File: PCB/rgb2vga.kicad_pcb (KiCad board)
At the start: 2 copper layers, 73.7 x 55.9 mm, 41 parts, among them U1 LM1881

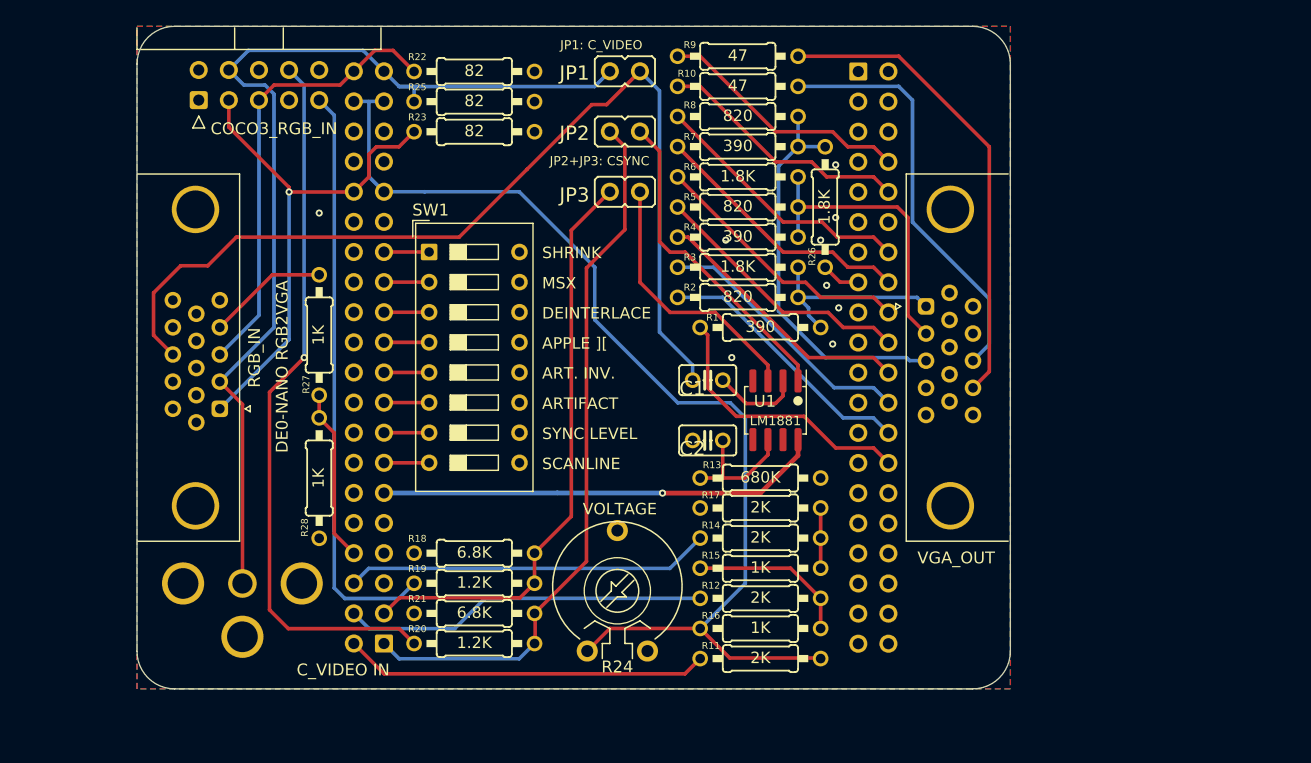
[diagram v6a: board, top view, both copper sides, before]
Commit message: layout grid alignmen
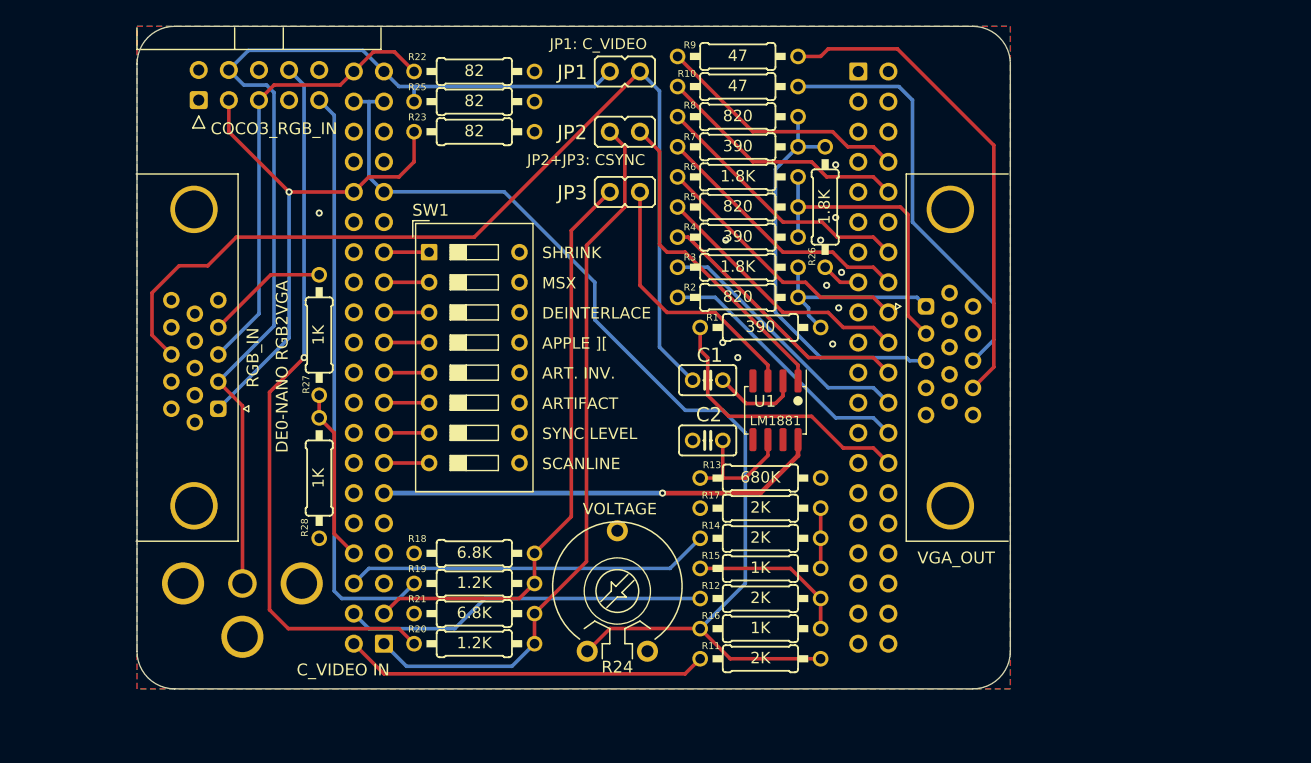
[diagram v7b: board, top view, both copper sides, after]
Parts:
- moved RGB_IN 0.13 mm to (109.2, 105.3)
- turned JP2 to 90 degrees
- turned JP3 to 90 degrees
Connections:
- JP2 pad 1: _HSYNC -> N$3
- JP2 pad 2: N$3 -> _HSYNC
- JP3 pad 1: _VSYNC -> N$2
- JP3 pad 2: N$2 -> _VSYNC
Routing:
- net DIFF_N: track 92.5 -> 91.1 mm
- net _VS: track 40.2 -> 41.3 mm
- net DIFFG: track 85.7 -> 84.7 mm
- net GND: vias 9 -> 11

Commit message: link schematic to pcb, remove unused footprints and models
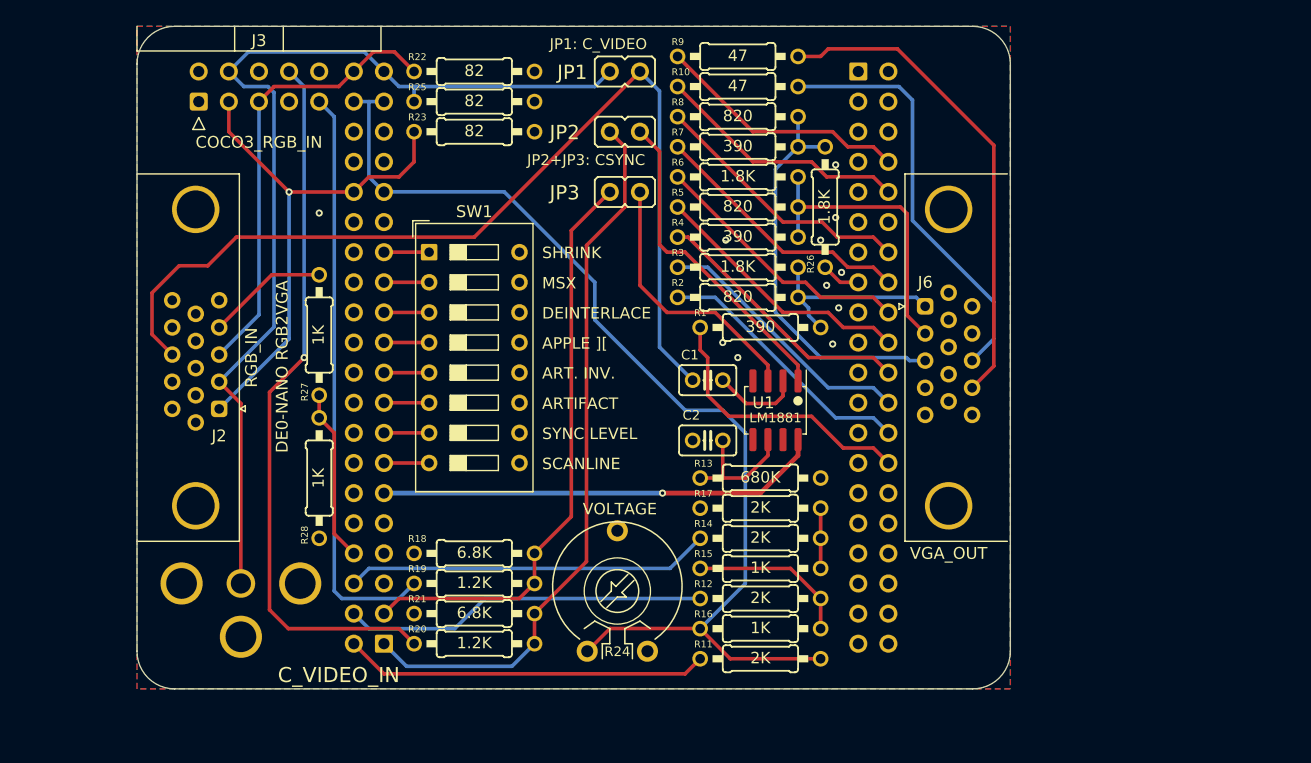
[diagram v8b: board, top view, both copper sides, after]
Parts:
- removed COCO3_RGB_IN: , 000_LOCAL:IDC-Header_2x05_P2.54mm_Horizontal
- removed C_VIDEO_IN: RCA female 90 degree, 000_LOCAL:RCA
- removed GPIO0, GPIO1: , 000_LOCAL:PinSocket_2x20_P2.54mm_Vertical
- removed RGB_IN, VGA_OUT: , 000_LOCAL:DSUB-15-HD_Female_Horizontal_P2.29x1.98mm_EdgePinOffset3.03mm_Housed_MountingHolesOffset4.94mm
- added J1: GPIO_0, 000_LOCAL:PinSocket_2x20_P2.54mm_Vertical, B.Cu at (123.2, 125.1)
- added J2: RGB_IN, 000_LOCAL:DE15F_Horiz_P2.29x1.98_3.03mm, F.Cu at (107.3, 101.0)
- added J3: COCO3_RGB_IN, 000_LOCAL:IDC-Header_2x05_P2.54mm_Horizontal, F.Cu at (107.6, 79.4)
- added J4: C_VIDEO_IN, 000_LOCAL:RCA, F.Cu at (111.1, 120.0)
- added J5: GPIO_1, 000_LOCAL:PinSocket_2x20_P2.54mm_Vertical, B.Cu at (163.2, 76.8)
- added J6: VGA_OUT, 000_LOCAL:DE15F_Horiz_P2.29x1.98_3.03mm, F.Cu at (170.8, 101.0)
- C1, C2: value 104 -> 0.1u
- JP1, JP2, JP3: value (none) -> Jumper_2_Open
- R24: value 30K -> 10K
- SW1: value (none) -> SW_DIP_x08
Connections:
- net BLUE renamed /BLUE
- net CSYNC renamed /CSYNC
- net DIFFG renamed /DIFFG
- net DIFF_N renamed /DIFF_N
- net GREEN renamed /GREEN
- net RED renamed /RED
- net RSET renamed /RSET
- net _HSYNC renamed /_HSYNC
- net _VSYNC renamed /_VSYNC
- R1 pad 1: R2 -> /R2
- R10 pad 1: HS -> /HS
- R10 pad 2: _HS -> Net-(J6-Pad13)
- R11 pad 1: D2 -> /D2
- R12 pad 1: D1 -> /D1
- R14 pad 1: D0 -> /D0
- R19 pad 1: VSYNC -> /VSYNC
- R2 pad 1: R1 -> /R1
- R20 pad 1: HSYNC -> /HSYNC
- R22 pad 1: DIFFB -> /DIFFB
- R23 pad 1: DIFFR -> /DIFFR
- R26 pad 1: (no net) -> /B0
- R27 pad 1: (no net) -> /_BRIGHT
- R27 pad 2: (no net) -> /BRIGHT
- R28 pad 2: (no net) -> /_BRIGHT
- R3 pad 1: R0 -> /R0
- R4 pad 1: G2 -> /G2
- R5 pad 1: G1 -> /G1
- R6 pad 1: G0 -> /G0
- R7 pad 1: B1 -> /B2
- R8 pad 1: B0 -> /B1
- R9 pad 1: VS -> /VS
- R9 pad 2: _VS -> Net-(J6-Pad14)
- U1 pad 8: VCC -> +5V
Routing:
- net HSYNC: track 60.6 -> 0.00 mm, vias 1 -> 0
- net /HSYNC: track 0.00 -> 60.5 mm, vias 0 -> 1
- net VSYNC: track 49.4 -> 0.00 mm
- net /VSYNC: track 0.00 -> 49.3 mm
- net DIFFR: track 44.7 -> 0.00 mm, vias 1 -> 0
- net /DIFFR: track 0.00 -> 44.6 mm, vias 0 -> 1
- net Net-(J6-Pad14): track 0.00 -> 41.3 mm
- net _VS: track 41.3 -> 0.00 mm
- net DIFFB: track 38.3 -> 0.00 mm
- net /DIFFB: track 0.00 -> 38.2 mm
- net VCC: track 37.6 -> 0.00 mm, vias 1 -> 0
- net +5V: track 0.00 -> 37.6 mm, vias 0 -> 1
- net Net-(J6-Pad13): track 0.00 -> 35.7 mm
- net _HS: track 35.7 -> 0.00 mm
- net D2: track 30.8 -> 0.00 mm
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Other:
- board text removed: "C_VIDEO IN"
